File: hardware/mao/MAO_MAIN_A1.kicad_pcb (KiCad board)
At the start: 4 copper layers, 58 x 56 mm, 140 parts, among them J101 USB-C, J102 BAT, J201 TAG, J301 LCD, J501 LRA, Q101 AO3401A, Q102 2N7002, Q302 DMG2302UKQ, Q501 AO3400A, SW301 SKQGADE010, U101 TPD2E2U06, U102 BQ25185DLHR, U103 MAX17048G+T10, U104 TPS62840DLCR, U105 TPS22916CYFPR, U201 ESP32-S3-MINI-1-N8, U301 DRV5012AEDMRR, U302 DRV5012AEDMRR, U304 TLV9061IDBVR, U401 ICM-42670-P, U402 VL53L4CDV0DH/1, U501 MAX98357AETE+T, U502 DRV2605LDGST, U503 IRM-H638T/TR2, U504 TPS22916CYFPR

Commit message: A1: 0.8 mm VBUS feed, BQ25185 EP vias, TPS62840 GND via, second module 3V3 via (design review 2026-10-06, findings 4-6)
- VBUS from the L3 strip to the charger's IN via: 0.4 -> 0.8 mm on L3, re-drawn east to clear the vias beside it;
  F link to C101 / U102.10 0.4-0.5 mm (0.3 mm into the 0.2 mm pin). The router's VBUS_SENSE run under the buck moves
  0.35 mm east.
- U102 (BQ25185) exposed pad: two 0.5/0.2 mm GND vias in its south half (the north half is over R122 on B).
- U104 (TPS62840): one 0.5/0.2 mm GND via 0.6 mm from GND pin 1 (F ground of R103/R104, B ground web of pins 1/3/6
  and C105.2); no other site round the part. Module 3V3: a second +3V3 plane via between C202 and C201.
DRC 0 / 0 / 0, planes continuous (route_review.py 4 5 6).

Co-Authored-By: Claude Opus 5.5 <noreply@anthropic.com>
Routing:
- net GND: track 117.5 -> 118.0 mm, vias 88 -> 91
- net +3V3: vias 26 -> 27
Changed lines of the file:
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@@
 	)
 	(via
+		(at 59.635 37.8)
+		(size 0.5)
+		(drill 0.2)
+		(layers "F.Cu" "B.Cu")
+		(locked yes)
+		(net "GND")
+	)
+	(via
 		(at 23.983094 40.78693)
 		(size 0.6)
@@
 	)
 	(via
+		(at 59.185 37.8)
+		(size 0.5)
+		(drill 0.2)
+		(layers "F.Cu" "B.Cu")
+		(locked yes)
+		(net "GND")
+	)
+	(via
 		(at 59.41 36.925)
 		(size 0.6)
@@
 	)
 	(via
+		(at 56.05 37.65)
+		(size 0.5)
+		(drill 0.2)
+		(layers "F.Cu" "B.Cu")
+		(locked yes)
+		(net "GND")
+	)
+	(via
 		(at 36.4 27.941)
 		(size 0.6)
@@
 	)
 	(segment
+		(start 56.05 37.65)
+		(end 56.4 38)
+		(width 0.3)
+		(locked yes)
+		(layer "B.Cu")
+		(net "GND")
+	)
+	(segment
 		(start 46.75 27.8)
 		(end 45.68 27.8)
@@
 	)
 	(via
+		(at 40.7 69.55)
+		(size 0.6)
+		(drill 0.3)
+		(layers "F.Cu" "B.Cu")
+		(locked yes)
+		(net "+3V3")
+	)
+	(via
 		(at 39.150861 33.803513)
 		(size 0.6)
@@
 	)
 	(segment
-		(start 58.31 39.025)
+		(start 59 40.22)
 		(end 58.31 40.22)
-		(width 0.3)
+		(width 0.5)
 		(locked yes)
 		(layer "F.Cu")
@@
 	)
 	(segment
-		(start 59 40.22)
-		(end 59 42.1)
+		(start 58.31 39.5)
+		(end 58.31 39.025)
 		(width 0.3)
 		(locked yes)
@@
 	)
 	(segment
-		(start 58.31 40.22)
+		(start 59 42.1)
 		(end 59 40.22)
-		(width 0.3)
+		(width 0.4)
+		(locked yes)
+		(layer "F.Cu")
+		(net "VBUS")
+	)
+	(segment
+		(start 58.31 40.22)
+		(end 58.31 39.5)
+		(width 0.5)
 		(locked yes)
 		(layer "F.Cu")
@@
 	)
 	(segment
-		(start 59 42.1)
-		(end 59 38)
-		(width 0.4)
+		(start 57.3 37.8)
+		(end 59 39.5)
+		(width 0.8)
 		(locked yes)
 		(layer "In2.Cu")
@@
 	)
 	(segment
-		(start 55 34)
-		(end 55 32.7)
-		(width 0.4)
+		(start 57.3 35.3)
+		(end 57.3 37.8)
+		(width 0.8)
 		(locked yes)
 		(layer "In2.Cu")
@@
 	)
 	(segment
-		(start 59 38)
-		(end 55 34)
-		(width 0.4)
+		(start 54.9 32.9)
+		(end 57.3 35.3)
+		(width 0.8)
+		(locked yes)
+		(layer "In2.Cu")
+		(net "VBUS")
+	)
+	(segment
+		(start 59 39.5)
+		(end 59 42.1)
+		(width 0.8)
 		(locked yes)
 		(layer "In2.Cu")
@@
 	)
 	(segment
-		(start 56.25 36.9)
-		(end 55 36.9)
+		(start 55 36.9)
+		(end 56.6 36.9)
+		(width 0.2)
+		(locked yes)
+		(layer "In2.Cu")
+		(net "VBUS_SENSE")
+	)
+	(segment
+		(start 56.25 41)
+		(end 56.25 41.6)
+		(width 0.2)
+		(locked yes)
+		(layer "In2.Cu")
+		(net "VBUS_SENSE")
+	)
+	(segment
+		(start 56.6 36.9)
+		(end 56.6 40.65)
 		(width 0.2)
+		(locked yes)
 		(layer "In2.Cu")
 		(net "VBUS_SENSE")
 	)
 	(segment
-		(start 56.25 41.6)
-		(end 56.25 36.9)
+		(start 56.6 40.65)
+		(end 56.25 41)
 		(width 0.2)
+		(locked yes)
 		(layer "In2.Cu")
 		(net "VBUS_SENSE")

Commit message: A1 outputs after the design review: silk (USB / IO39 pad names, Q102), fab package (BOM 49 lines / 100 parts with LCSC numbers, CPL, gerbers, drill, assembly drawings), layer plots and renders
Silk re-run leaves every easter egg where it was (102 egg items identical); check_silk_text 76 texts, 0 findings;
mech_check 140 parts, 0 findings (Q102 1.2 mm under the panel, at the 1.2 mm limit). FAB-NOTES: order JLC Standard
PCBA (0.4 mm WCSP U105/U504, both sides), U102 EP vias, the USB pair geometry. Renders: same views and sizes
(top/bottom 1800x1800, iso -50,0,25 / iso-back 130,0,25 perspective zoom 0.85 1800x1400, edges 2000x420 zoom 3).

Co-Authored-By: Claude Opus 5.5 <noreply@anthropic.com>
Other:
- board text added: "IO39"
- board text removed: "IO2"

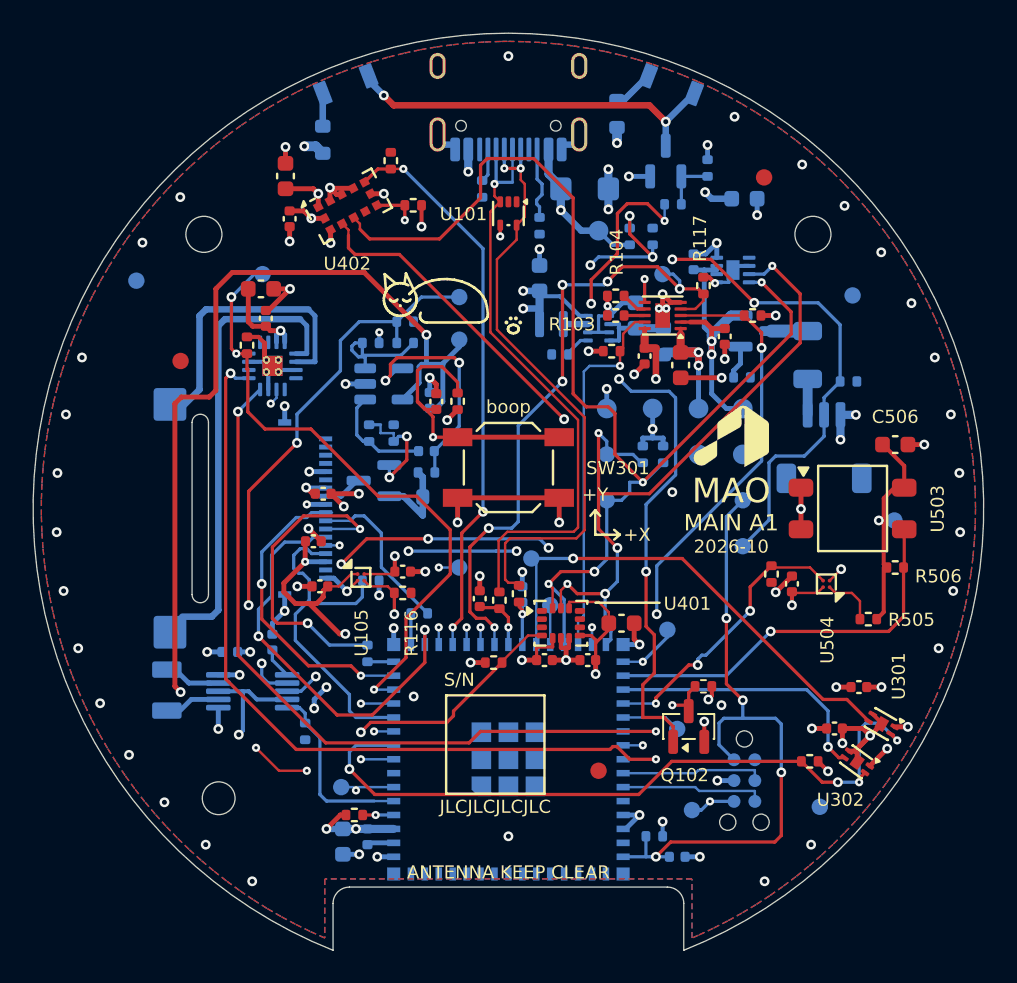
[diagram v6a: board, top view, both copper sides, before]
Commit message: A1 face press: tripod of three ALPS SKQGAFE010 (owner decision 2026-10-06)
Three 0.98 N / 0.25 mm / 1.5 mm SKQG switches (C202424) in parallel on PRESS_N
at 70 / 190 / 310 deg (r 17.6 / 14.5 / 14.5) replace the single SKQGADE010 at
the centre; no pin or firmware change. The 3 o'clock half of the panel area is
the tail well, the IR receiver and the charger, so the 70 deg switch takes the
only pocket there at r 17.6. Surgical: sync_fields --add, route_tripod.py
place / rip / add (I2C pair through SW301's channel, PRESS_N to each switch,
IMU_INT1 / AMP_BCLK / HALL_FAST round SW302, GND vias); SKQG legs jumpered
inside the part (build_pcb.JUMPERED_LEGS). Maker mark and S/N field find a
clear spot under the panel. DRC 0/0/0, planes one piece, mech 0 findings.

Co-Authored-By: Claude Opus 5.5 <noreply@anthropic.com>
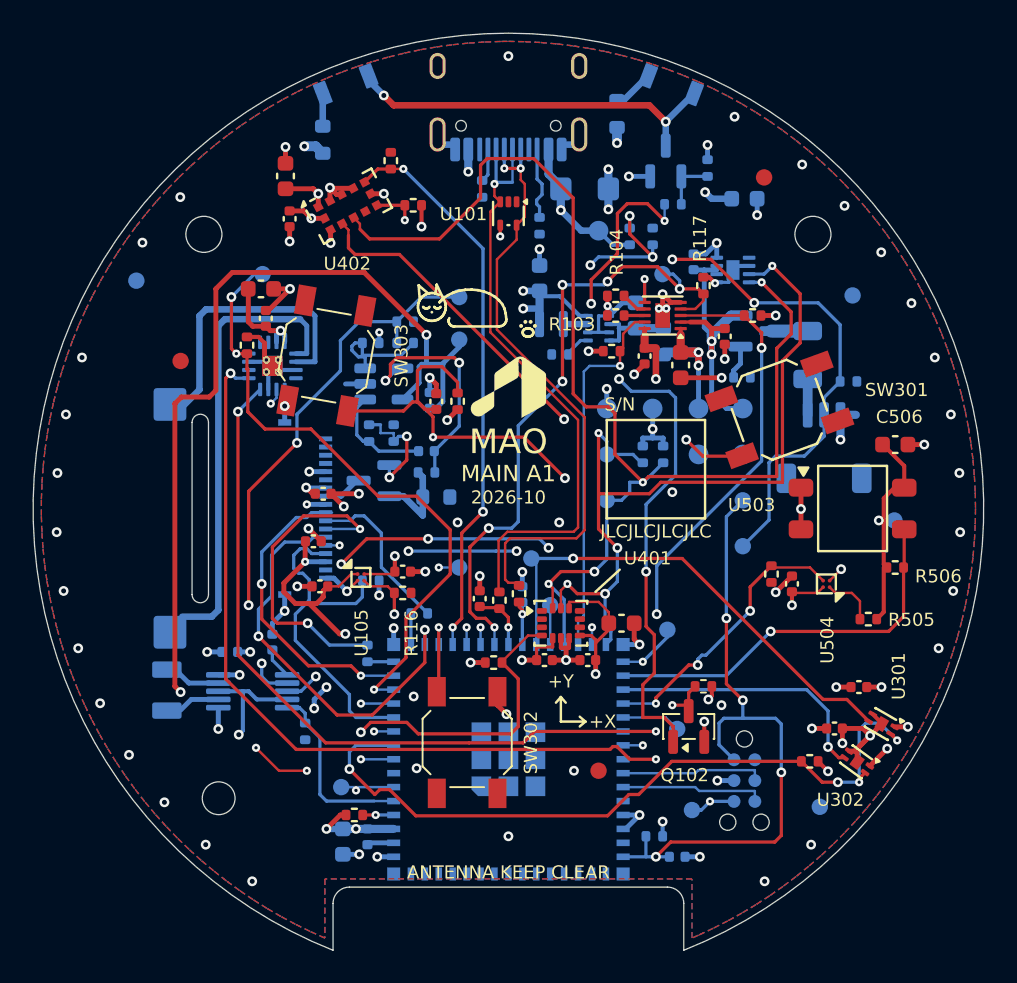
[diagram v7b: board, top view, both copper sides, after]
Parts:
- added SW302: SKQGAFE010, Button_Switch_SMD:SW_SPST_SKQG_WithStem, F.Cu at (47.5, 64.3)
- added SW303: SKQGAFE010, Button_Switch_SMD:SW_SPST_SKQG_WithStem, F.Cu at (38.9, 40.7)
- SW301: value SKQGADE010 -> SKQGAFE010
- moved SW301 16.9 mm to (66.5, 44.0), turned to -160 degrees
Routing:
- net PRESS_N: track 31.2 -> 52.5 mm, vias 3 -> 5
- net GND: track 118.0 -> 110.4 mm, vias 91 -> 92
- net I2C_SDA: track 99.9 -> 104.5 mm
- net I2C_SCL: track 98.4 -> 102.7 mm
- net IMU_INT1: track 17.6 -> 21.7 mm
- net HALL_FAST: track 44.4 -> 45.8 mm
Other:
- board text removed: "boop"
